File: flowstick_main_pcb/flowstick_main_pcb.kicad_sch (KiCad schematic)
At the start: 53 parts, among them J1 USB_C_Receptacle_USB2.0_16P, J2 Conn_01x01_Pin, J3 Conn_01x01_Pin, J4 Conn_01x01_Pin, J5 Conn_01x01_Pin, SW1 SW_Push, U1 ESP32-S3, U2 MP3414A, U3 LM3671, U4 BQ21040DBV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

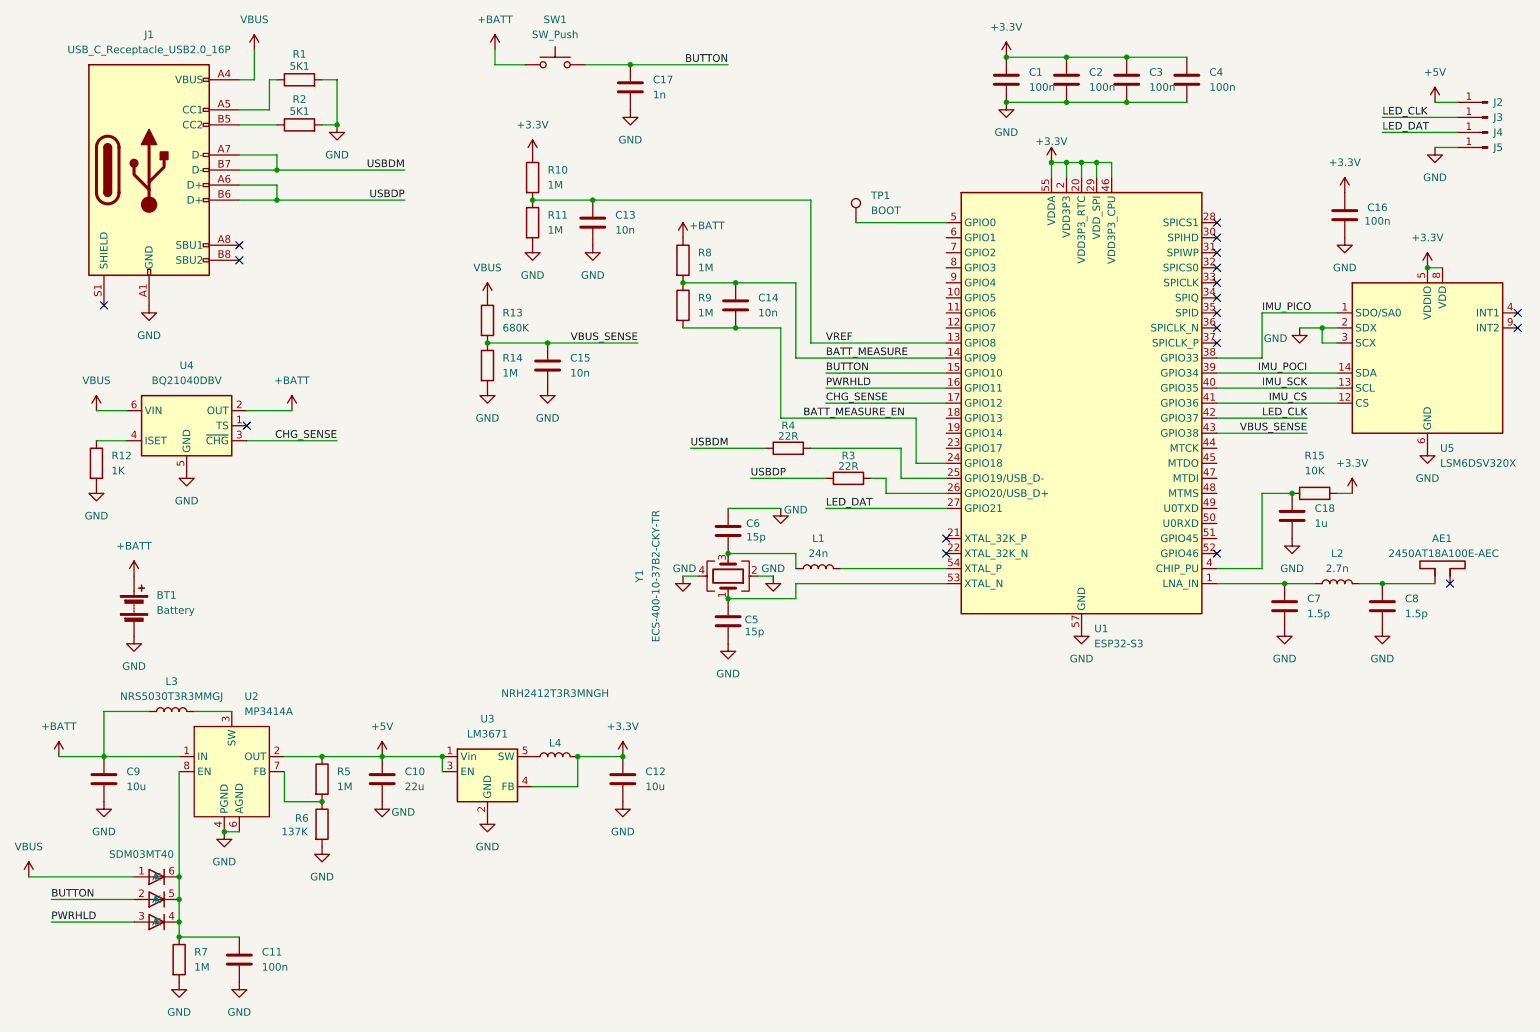
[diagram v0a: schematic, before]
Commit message: work on rev2 + panelize LED strips
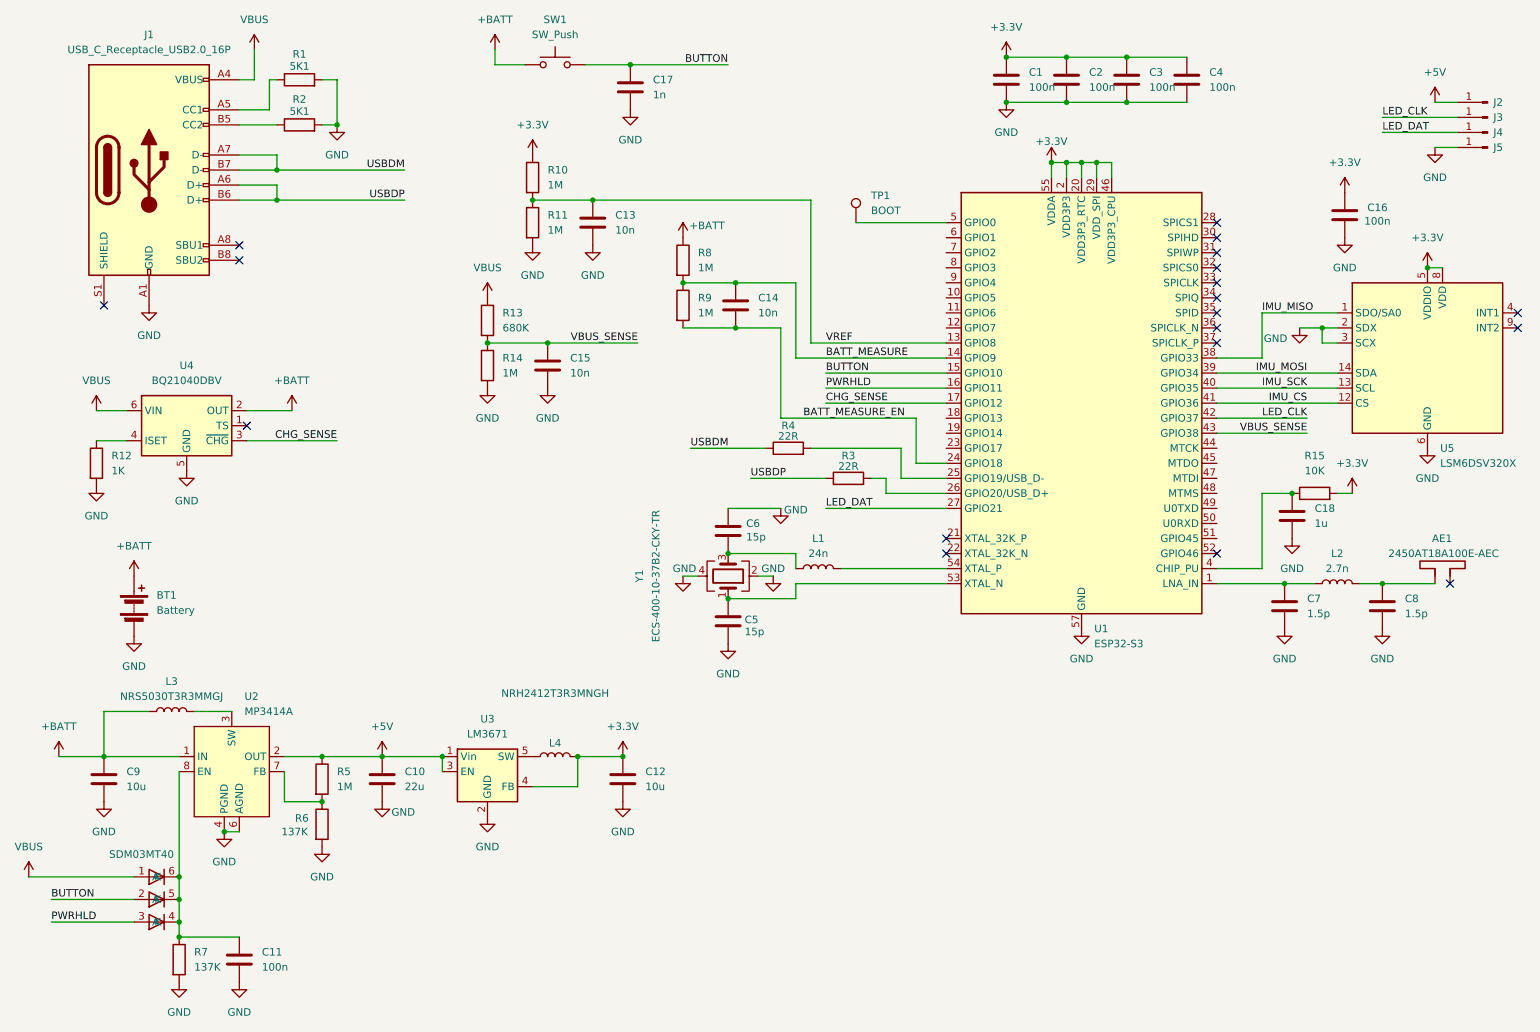
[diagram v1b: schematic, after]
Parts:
- R7: value 1M -> 137K
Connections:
- net IMU_PICO renamed IMU_MISO
- net IMU_POCI renamed IMU_MOSI
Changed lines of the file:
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@@
 		)
 	)
-	(label "IMU_PICO"
+	(label "IMU_MISO"
 		(at 228.6 71.12 0)
 		(effects
@@
 		)
 	)
-	(label "IMU_POCI"
+	(label "IMU_MOSI"
 		(at 236.22 81.28 180)
 		(effects
@@
 			)
 		)
-		(property "Value" "1M"
+		(property "Value" "137K"
 			(at 48.26 181.6099 0)
 			(effects
